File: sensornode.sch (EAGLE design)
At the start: 73 parts, among them IC1 CP2104, Q1 mmbt2222, Q2 mmbt2222, Q3 DMG3415U, SW2 KMR2, U1 TSL2591, U2 AP2112-3.3, U3 MCP73831T-2ACI/OT, U4 BMEx80, X2 ESP32_WROOM32_SKINNY, X4 20329

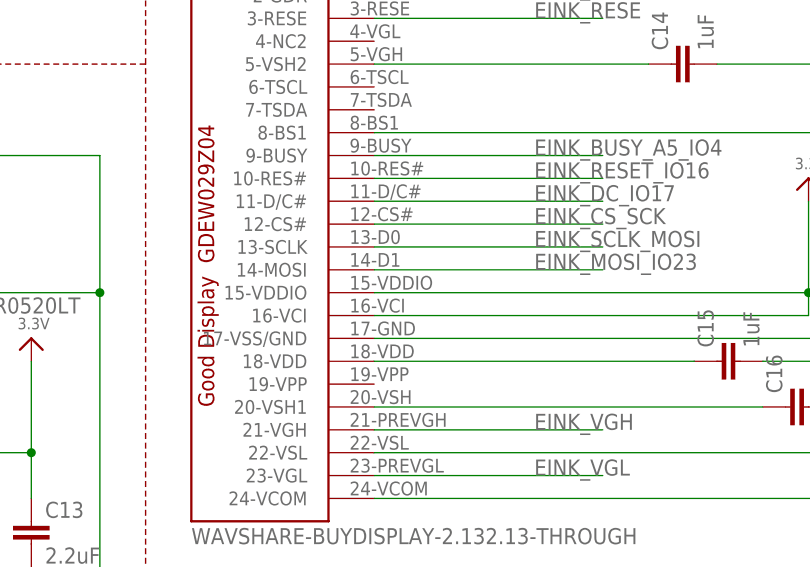
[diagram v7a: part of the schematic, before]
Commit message: Updating the FPC + part for the e-ink screen
Think I had the pinout on the FPC backwards.  This should flip it
and move a bunch of pieces around as a result
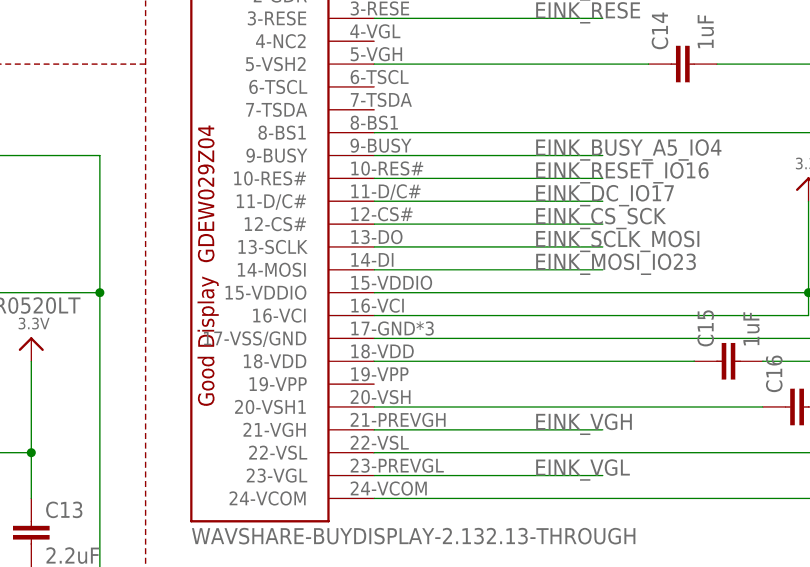
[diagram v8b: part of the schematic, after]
